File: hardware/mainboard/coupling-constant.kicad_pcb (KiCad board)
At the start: 2 copper layers, 72.5 x 33.5 mm, 38 parts, among them J1 DC IN, J2 Input, J3 Output, U1 TC1044SxOA, U2 TL072

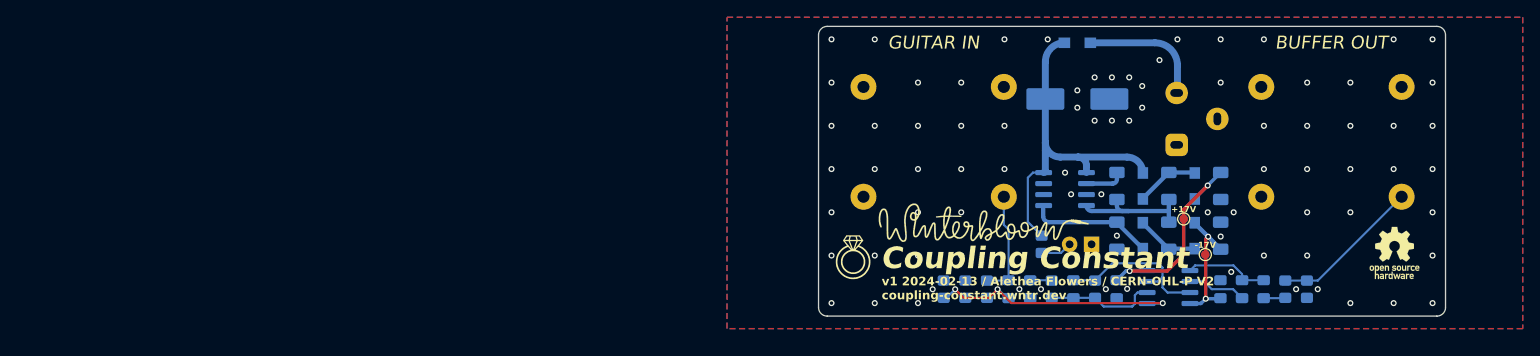
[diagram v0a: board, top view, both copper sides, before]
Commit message: hardware: revision 2
- Swap TL072 for NJM2068
- Swap footprint for one compatible with SOIC-8 and DMP-8, making it easier to swap op-amps
- Remove feedback cap in output amplifier, it's not needed and has only caused problems.
- Update everything to KiCAD 8
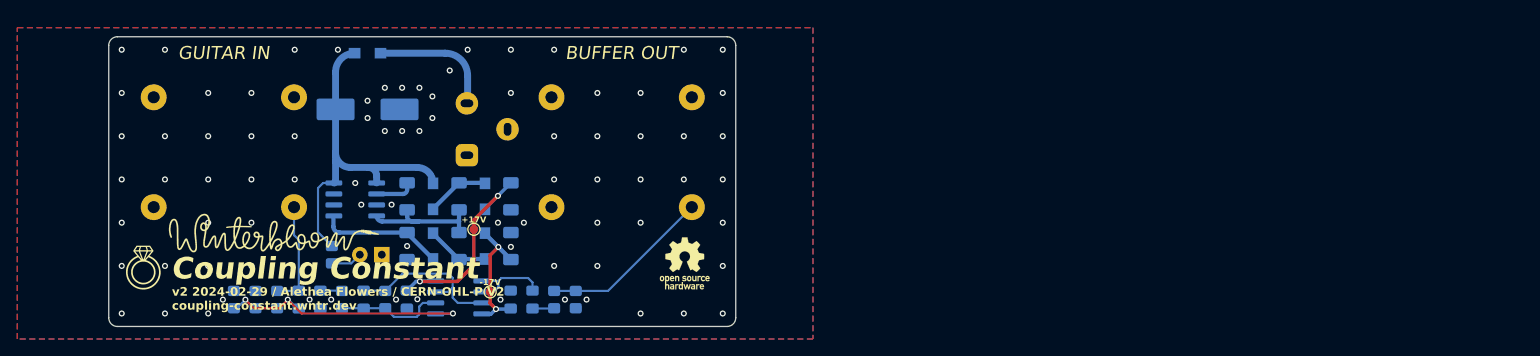
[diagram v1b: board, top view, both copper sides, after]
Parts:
- removed C13: TODO, winterbloom:C_0805_HandSolder
- U2: value TL072 -> NJM2068; footprint Package_SO:SOIC-8_3.9x4.9mm_P1.27mm -> winterbloom:SOIC-8+DMP-8_5mmx5mm_P1.27mm
- moved C14 84.6 mm to (88.6, 119.0)
- moved R6 84.6 mm to (91.1, 119.0)
- moved R7 84.6 mm to (93.6, 119.0)
- moved TP2 82.8 mm to (83.7, 118.2)
- moved C10 82.1 mm to (69.1, 119.0)
- moved C11 82.1 mm to (86.1, 119.0)
- moved C12 82.1 mm to (74.1, 119.0)
- moved C5 82.1 mm to (86.1, 112.9)
- moved C6 82.1 mm to (80.1, 112.9)
- moved C7 82.1 mm to (74.1, 112.9)
- moved C8 82.1 mm to (61.6, 119.0)
- moved C9 82.1 mm to (64.1, 119.0)
- moved D4 82.1 mm to (83.1, 112.9)
- moved D5 82.1 mm to (77.1, 112.9)
- moved R1 82.1 mm to (54.1, 119.0)
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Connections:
- C14 pad 1: Net-(C13-Pad2) -> Net-(U2A--)
- U2 pad 1: Net-(C13-Pad2) -> Net-(U2A--)
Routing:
- net Net-(C13-Pad2): track 9.90 -> 0.00 mm
- net Net-(U2A--): track 6.82 -> 10.1 mm
- net /guitar out: track 17.5 -> 19.9 mm
- net VEE: track 15.3 -> 15.9 mm
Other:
- board text added: "PCB Specifications: - Dimensions: 72.5mm x 33.5mm - Thickness: 1.6mm - Layers: 2 - Min. track width: 0.2mm / 7 mil - Min. track spacing: 0.2mm / 7 mil - Min. drill: 0.4mm - Mask: Black - Silk: White - Surface finish: ENIG - Copper weight: 1oz - Substrate: FR4 TG 140 or better - UL Marking: Bottom silk"
